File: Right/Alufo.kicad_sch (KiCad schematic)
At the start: 22 parts, among them J2 USB_C_Receptacle_USB2.0_16P_2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, J4 USB_C_Receptacle_USB2.0_16P_2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, SW10 BOOT, U2 CH552T, U4 USBLC6-2P6, U6 USBLC6-2P6

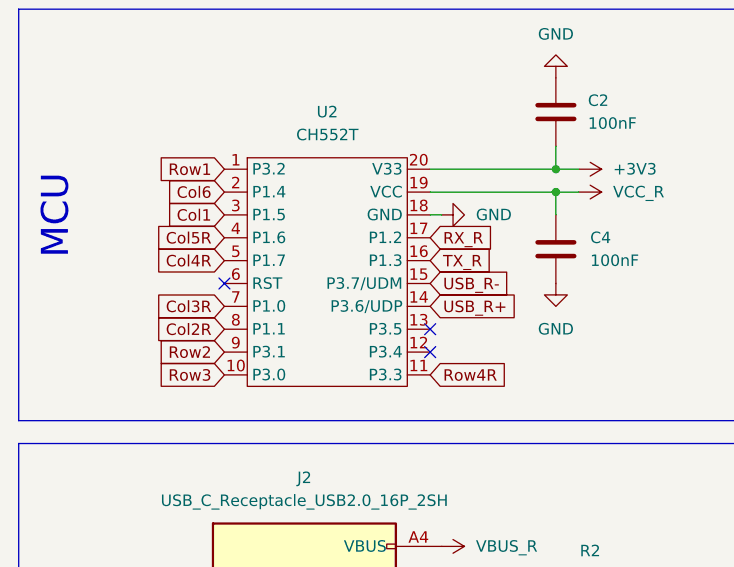
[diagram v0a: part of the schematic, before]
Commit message: Route Row 2 under upper 0Ω resistors
TODO: Reconnect Column 6 to thumb row
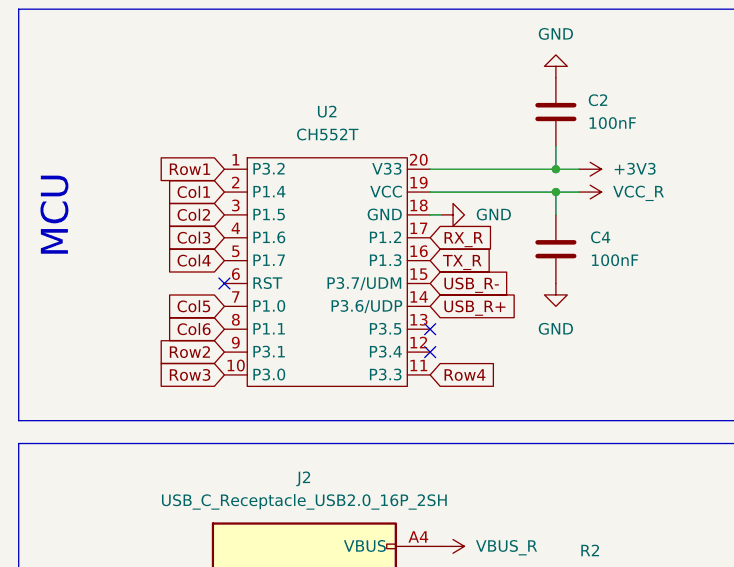
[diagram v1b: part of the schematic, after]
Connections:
- net Col2R is gone; now on net Col6: U2.8 (P1.1)
- net Col1: now also U2.2 (P1.4); no longer U2.3 (P1.5)
- net Col6: no longer U2.2 (P1.4)
- net Col3R renamed Col5
- net Col4R renamed Col4
- net Col5R renamed Col3
- net Row4R renamed Row4
- new net Col2: U2.3 (P1.5)
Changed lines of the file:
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@@
 		)
 	)
-	(global_label "Col5R"
+	(global_label "Col3"
 		(shape input)
 		(at 38.1 50.8 180)
@@
 		)
 		(property "Intersheetrefs" "${INTERSHEET_REFS}"
-			(at 29.5511 50.8 0)
+			(at 30.8211 50.8 0)
 			(effects
 				(font
@@
 		)
 	)
-	(global_label "Col4R"
+	(global_label "Col4"
 		(shape input)
 		(at 38.1 53.34 180)
@@
 		)
 		(property "Intersheetrefs" "${INTERSHEET_REFS}"
-			(at 29.5511 53.34 0)
-			(effects
-				(font
-					(size 1.27 1.27)
-				)
-				(justify right)
-				(hide yes)
-			)
-		)
-	)
-	(global_label "Row4R"
+			(at 30.8211 53.34 0)
+			(effects
+				(font
+					(size 1.27 1.27)
+				)
+				(justify right)
+				(hide yes)
+			)
+		)
+	)
+	(global_label "Row4"
 		(shape input)
 		(at 60.96 66.04 0)
@@
 		)
 		(property "Intersheetrefs" "${INTERSHEET_REFS}"
-			(at 70.1742 66.04 0)
-			(effects
-				(font
-					(size 1.27 1.27)
-				)
-				(justify left)
-				(hide yes)
-			)
-		)
-	)
-	(global_label "Col2R"
+			(at 68.9042 66.04 0)
+			(effects
+				(font
+					(size 1.27 1.27)
+				)
+				(justify left)
+				(hide yes)
+			)
+		)
+	)
+	(global_label "Col6"
 		(shape input)
 		(at 38.1 60.96 180)
@@
 		)
 		(property "Intersheetrefs" "${INTERSHEET_REFS}"
-			(at 29.5511 60.96 0)
+			(at 30.8211 60.96 0)
 			(effects
 				(font
@@
 		)
 	)
+	(global_label "Col2"
+		(shape input)
+		(at 38.1 48.26 180)
+		(fields_autoplaced yes)
+		(effects
+			(font
+				(size 1.27 1.27)
+			)
+			(justify right)
+		)
+		(property "Intersheetrefs" "${INTERSHEET_REFS}"
+			(at 30.8211 48.26 0)
+			(effects
+				(font
+					(size 1.27 1.27)
+				)
+				(justify right)
+				(hide yes)
+			)
+		)
+	)
+	(global_label "RX_PR"
+		(shape input)
+		(at 64.77 170.18 0)
+		(fields_autoplaced yes)
+		(effects
+			(font
+				(size 1.27 1.27)
+			)
+			(justify left)
+		)
+		(property "Intersheetrefs" "${INTERSHEET_REFS}"
+			(at 73.7423 170.18 0)
+			(effects
+				(font
+					(size 1.27 1.27)
+				)
+				(justify left)
+				(hide yes)
+			)
+		)
+	)
+	(global_label "USB_R-"
+		(shape input)
+		(at 115.57 115.57 180)
+		(fields_autoplaced yes)
+		(effects
+			(font
+				(size 1.27 1.27)
+			)
+			(justify right)
+		)
+		(property "Intersheetrefs" "${INTERSHEET_REFS}"
+			(at 104.9648 115.57 0)
+			(effects
+				(font
+					(size 1.27 1.27)
+				)
+				(justify right)
+				(hide yes)
+			)
+		)
+	)
+	(global_label "TX_PR"
+		(shape input)
+		(at 64.77 165.1 0)
+		(fields_autoplaced yes)
+		(effects
+			(font
+				(size 1.27 1.27)
+			)
+			(justify left)
+		)
+		(property "Intersheetrefs" "${INTERSHEET_REFS}"
+			(at 73.4399 165.1 0)
+			(effects
+				(font
+					(size 1.27 1.27)
+				)
+				(justify left)
+				(hide yes)
+			)
+		)
+	)
+	(global_label "BOOT"
+		(shape input)
+		(at 167.64 109.22 180)
+		(fields_autoplaced yes)
+		(effects
+			(font
+				(size 1.27 1.27)
+			)
+			(justify right)
+		)
+		(property "Intersheetrefs" "${INTERSHEET_REFS}"
+			(at 159.7562 109.22 0)
+			(effects
+				(font
+					(size 1.27 1.27)
+				)
+				(justify right)
+				(hide yes)
+			)
+		)
+	)
+	(global_label "Row1"
+		(shape input)
+		(at 38.1 43.18 180)
+		(fields_autoplaced yes)
+		(effects
+			(font
+				(size 1.27 1.27)
+			)
+			(justify right)
+		)
+		(property "Intersheetrefs" "${INTERSHEET_REFS}"
+			(at 30.1558 43.18 0)
+			(effects
+				(font
+					(size 1.27 1.27)
+				)
+				(justify right)
+				(hide yes)
+			)
+		)
+	)
 	(global_label "Col1"
 		(shape input)
-		(at 38.1 48.26 180)
-		(fields_autoplaced yes)
-		(effects
-			(font
-				(size 1.27 1.27)
-			)
-			(justify right)
-		)
-		(property "Intersheetrefs" "${INTERSHEET_REFS}"
-			(at 30.8211 48.26 0)
-			(effects
-				(font
-					(size 1.27 1.27)
-				)
-				(justify right)
-				(hide yes)
-			)
-		)
-	)
-	(global_label "RX_PR"
-		(shape input)
-		(at 64.77 170.18 0)
-		(fields_autoplaced yes)
-		(effects
-			(font
-				(size 1.27 1.27)
-			)
-			(justify left)
-		)
-		(property "Intersheetrefs" "${INTERSHEET_REFS}"
-			(at 73.7423 170.18 0)
-			(effects
-				(font
-					(size 1.27 1.27)
-				)
-				(justify left)
-				(hide yes)
-			)
-		)
-	)
-	(global_label "USB_R-"
-		(shape input)
-		(at 115.57 115.57 180)
-		(fields_autoplaced yes)
-		(effects
-			(font
-				(size 1.27 1.27)
-			)
-			(justify right)
-		)
-		(property "Intersheetrefs" "${INTERSHEET_REFS}"
-			(at 104.9648 115.57 0)
-			(effects
-				(font
-					(size 1.27 1.27)
-				)
-				(justify right)
-				(hide yes)
-			)
-		)
-	)
-	(global_label "TX_PR"
-		(shape input)
-		(at 64.77 165.1 0)
-		(fields_autoplaced yes)
-		(effects
-			(font
-				(size 1.27 1.27)
-			)
-			(justify left)
-		)
-		(property "Intersheetrefs" "${INTERSHEET_REFS}"
-			(at 73.4399 165.1 0)
-			(effects
-				(font
-					(size 1.27 1.27)
-				)
-				(justify left)
-				(hide yes)
-			)
-		)
-	)
-	(global_label "BOOT"
-		(shape input)
-		(at 167.64 109.22 180)
-		(fields_autoplaced yes)
-		(effects
-			(font
-				(size 1.27 1.27)
-			)
-			(justify right)
-		)
-		(property "Intersheetrefs" "${INTERSHEET_REFS}"
-			(at 159.7562 109.22 0)
-			(effects
-				(font
-					(size 1.27 1.27)
-				)
-				(justify right)
-				(hide yes)
-			)
-		)
-	)
-	(global_label "Row1"
-		(shape input)
-		(at 38.1 43.18 180)
-		(fields_autoplaced yes)
-		(effects
-			(font
-				(size 1.27 1.27)
-			)
-			(justify right)
-		)
-		(property "Intersheetrefs" "${INTERSHEET_REFS}"
-			(at 30.1558 43.18 0)
-			(effects
-				(font
-					(size 1.27 1.27)
-				)
-				(justify right)
-				(hide yes)
-			)
-		)
-	)
-	(global_label "Col6"
-		(shape input)
 		(at 38.1 45.72 180)
 		(fields_autoplaced yes)
@@
 		)
 	)
-	(global_label "Col3R"
+	(global_label "Col5"
 		(shape input)
 		(at 38.1 58.42 180)
@@
 		)
 		(property "Intersheetrefs" "${INTERSHEET_REFS}"
-			(at 29.5511 58.42 0)
-			(effects
-				(font
+			(at 30.8211 58.42 0)
+			(effects
+				(font

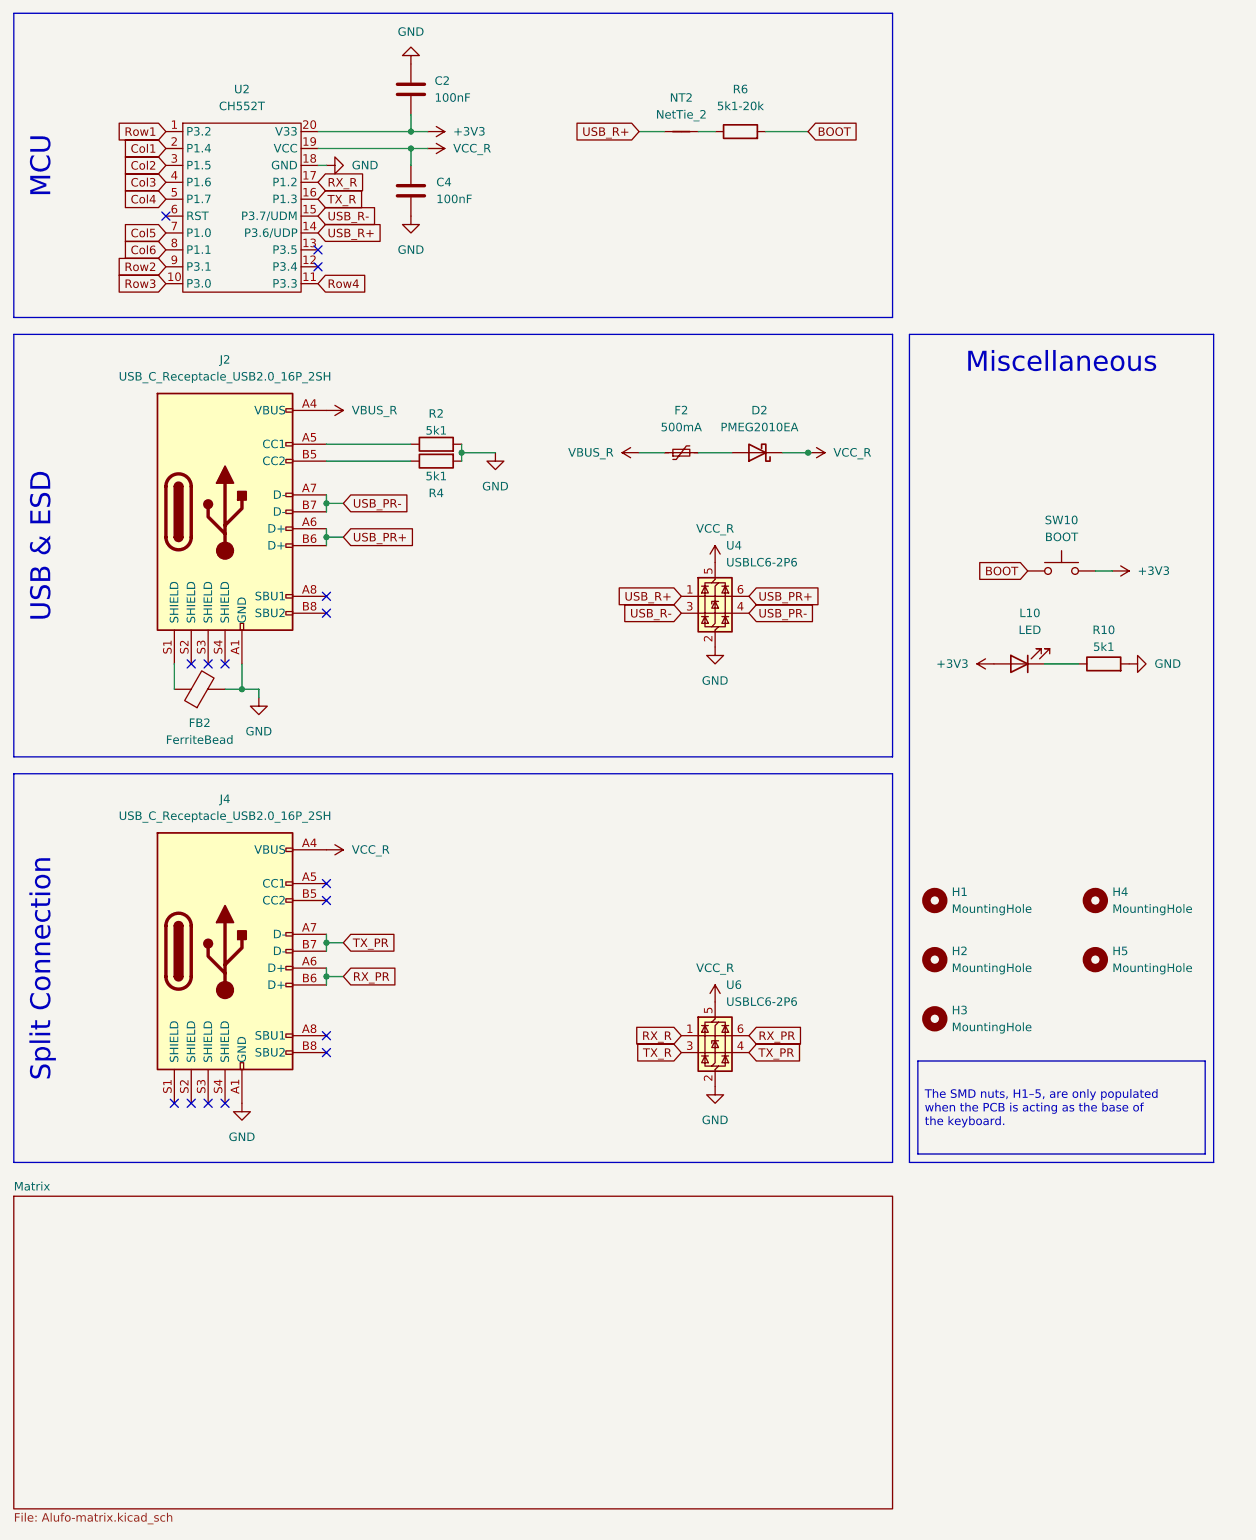
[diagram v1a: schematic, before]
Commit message: Remove “L” and “R” from all labels
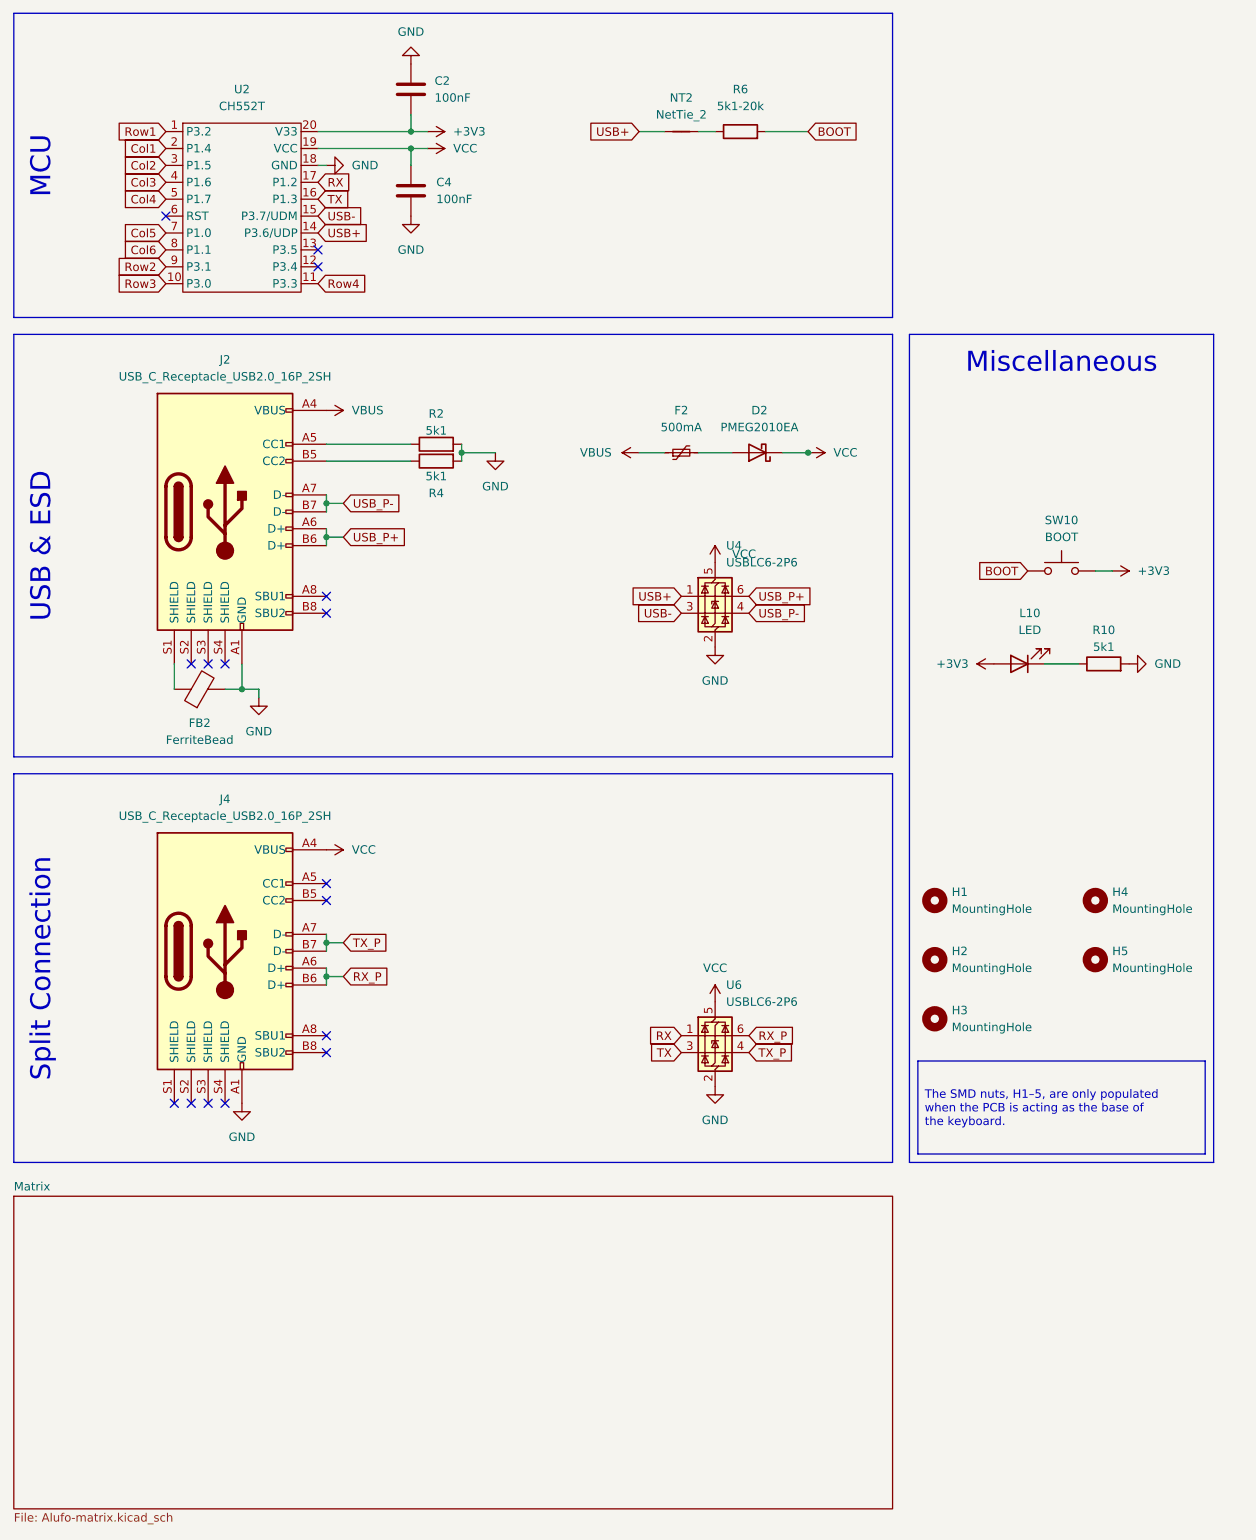
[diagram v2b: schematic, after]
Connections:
- net RX_PR renamed RX_P
- net RX_R renamed RX
- net TX_PR renamed TX_P
- net TX_R renamed TX
- net USB_PR+ renamed USB_P+
- net USB_PR- renamed USB_P-
- net USB_R+ renamed USB+
- net USB_R- renamed USB-
- net VBUS_R renamed VBUS
- net VCC_R renamed VCC
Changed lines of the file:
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@@
 		)
 	)
-	(global_label "USB_R-"
+	(global_label "USB-"
 		(shape input)
 		(at 60.96 55.88 0)
@@
 		)
 		(property "Intersheetrefs" "${INTERSHEET_REFS}"
-			(at 71.5652 55.88 0)
-			(effects
-				(font
-					(size 1.27 1.27)
-				)
-				(justify left)
-				(hide yes)
-			)
-		)
-	)
-	(global_label "RX_PR"
+			(at 69.3276 55.88 0)
+			(effects
+				(font
+					(size 1.27 1.27)
+				)
+				(justify left)
+				(hide yes)
+			)
+		)
+	)
+	(global_label "RX_P"
 		(shape input)
 		(at 125.73 179.07 0)
@@
 		)
 		(property "Intersheetrefs" "${INTERSHEET_REFS}"
-			(at 134.7023 179.07 0)
+			(at 133.4323 179.07 0)
 			(effects
 				(font
@@
 		)
 	)
-	(global_label "TX_R"
+	(global_label "TX"
 		(shape input)
 		(at 60.96 53.34 0)
@@
 		)
 		(property "Intersheetrefs" "${INTERSHEET_REFS}"
-			(at 68.3599 53.34 0)
-			(effects
-				(font
-					(size 1.27 1.27)
-				)
-				(justify left)
-				(hide yes)
-			)
-		)
-	)
-	(global_label "RX_R"
+			(at 66.1223 53.34 0)
+			(effects
+				(font
+					(size 1.27 1.27)
+				)
+				(justify left)
+				(hide yes)
+			)
+		)
+	)
+	(global_label "RX"
 		(shape input)
 		(at 115.57 179.07 180)
@@
 		)
 		(property "Intersheetrefs" "${INTERSHEET_REFS}"
-			(at 107.8677 179.07 0)
+			(at 110.1053 179.07 0)
 			(effects
 				(font
@@
 		)
 	)
-	(global_label "TX_PR"
+	(global_label "TX_P"
 		(shape input)
 		(at 125.73 181.61 0)
@@
 		)
 		(property "Intersheetrefs" "${INTERSHEET_REFS}"
-			(at 134.3999 181.61 0)
-			(effects
-				(font
-					(size 1.27 1.27)
-				)
-				(justify left)
-				(hide yes)
-			)
-		)
-	)
-	(global_label "USB_PR-"
+			(at 133.1299 181.61 0)
+			(effects
+				(font
+					(size 1.27 1.27)
+				)
+				(justify left)
+				(hide yes)
+			)
+		)
+	)
+	(global_label "USB_P-"
 		(shape input)
 		(at 64.77 99.06 0)
@@
 		)
 		(property "Intersheetrefs" "${INTERSHEET_REFS}"
-			(at 76.6452 99.06 0)
+			(at 75.3752 99.06 0)
 			(effects
 				(font
@@
 		)
 	)
-	(global_label "USB_PR-"
+	(global_label "USB_P-"
 		(shape input)
 		(at 125.73 115.57 0)
@@
 		)
 		(property "Intersheetrefs" "${INTERSHEET_REFS}"
-			(at 137.6052 115.57 0)
-			(effects
-				(font
-					(size 1.27 1.27)
-				)
-				(justify left)
-				(hide yes)
-			)
-		)
-	)
-	(global_label "USB_PR+"
+			(at 136.3352 115.57 0)
+			(effects
+				(font
+					(size 1.27 1.27)
+				)
+				(justify left)
+				(hide yes)
+			)
+		)
+	)
+	(global_label "USB_P+"
 		(shape input)
 		(at 125.73 113.03 0)
@@
 		)
 		(property "Intersheetrefs" "${INTERSHEET_REFS}"
-			(at 137.6052 113.03 0)
-			(effects
-				(font
-					(size 1.27 1.27)
-				)
-				(justify left)
-				(hide yes)
-			)
-		)
-	)
-	(global_label "USB_R+"
+			(at 136.3352 113.03 0)
+			(effects
+				(font
+					(size 1.27 1.27)
+				)
+				(justify left)
+				(hide yes)
+			)
+		)
+	)
+	(global_label "USB+"
 		(shape input)
 		(at 60.96 58.42 0)
@@
 		)
 		(property "Intersheetrefs" "${INTERSHEET_REFS}"
-			(at 71.5652 58.42 0)
+			(at 69.3276 58.42 0)
 			(effects
 				(font
@@
 		)
 	)
-	(global_label "USB_R+"
+	(global_label "USB+"
 		(shape input)
 		(at 109.22 43.18 180)
@@
 		)
 		(property "Intersheetrefs" "${INTERSHEET_REFS}"
-			(at 98.6148 43.18 0)
+			(at 100.8524 43.18 0)
 			(effects
 				(font
@@
 		)
 	)
-	(global_label "USB_PR+"
+	(global_label "USB_P+"
 		(shape input)
 		(at 64.77 104.14 0)
@@
 		)
 		(property "Intersheetrefs" "${INTERSHEET_REFS}"
-			(at 76.6452 104.14 0)
+			(at 75.3752 104.14 0)
 			(effects
 				(font
@@
 		)
 	)
-	(global_label "USB_R+"
+	(global_label "USB+"
 		(shape input)
 		(at 115.57 113.03 180)
@@
 		)
 		(property "Intersheetrefs" "${INTERSHEET_REFS}"
-			(at 104.9648 113.03 0)
+			(at 107.2024 113.03 0)
 			(effects
 				(font
@@
 		)
 	)
-	(global_label "RX_PR"
+	(global_label "RX_P"
 		(shape input)
 		(at 64.77 170.18 0)
@@
 		)
 		(property "Intersheetrefs" "${INTERSHEET_REFS}"
-			(at 73.7423 170.18 0)
-			(effects
-				(font
-					(size 1.27 1.27)
-				)
-				(justify left)
-				(hide yes)
-			)
-		)
-	)
-	(global_label "USB_R-"
+			(at 72.4723 170.18 0)
+			(effects
+				(font
+					(size 1.27 1.27)
+				)
+				(justify left)
+				(hide yes)
+			)
+		)
+	)
+	(global_label "USB-"
 		(shape input)
 		(at 115.57 115.57 180)
@@
 		)
 		(property "Intersheetrefs" "${INTERSHEET_REFS}"
-			(at 104.9648 115.57 0)
+			(at 107.2024 115.57 0)
 			(effects
 				(font
@@
 		)
 	)
-	(global_label "TX_PR"
+	(global_label "TX_P"
 		(shape input)
 		(at 64.77 165.1 0)
@@
 		)
 		(property "Intersheetrefs" "${INTERSHEET_REFS}"
-			(at 73.4399 165.1 0)
+			(at 72.1699 165.1 0)
 			(effects
 				(font
@@
 		)
 	)
-	(global_label "RX_R"
+	(global_label "RX"
 		(shape input)
 		(at 60.96 50.8 0)
@@
 		)
 		(property "Intersheetrefs" "${INTERSHEET_REFS}"
-			(at 68.6623 50.8 0)
-			(effects
-				(font
-					(size 1.27 1.27)
-				)
-				(justify left)
-				(hide yes)
-			)
-		)
-	)
-	(global_label "TX_R"
+			(at 66.4247 50.8 0)
+			(effects
+				(font
+					(size 1.27 1.27)
+				)
+				(justify left)
+				(hide yes)
+			)
+		)
+	)
+	(global_label "TX"
 		(shape input)
 		(at 115.57 181.61 180)
@@
 		)
 		(property "Intersheetrefs" "${INTERSHEET_REFS}"
-			(at 108.1701 181.61 0)
+			(at 110.4077 181.61 0)
 			(effects
 				(font
@@
 			)
 		)
-		(property "Value" "VCC_R"
+		(property "Value" "VCC"
 			(at 138.43 91.4399 90)
 			(effects
@@
 			)
 		)
-		(property "Value" "VCC_R"
+		(property "Value" "VCC"
 			(at 120.65 168.91 0)
 			(effects
@@
 			)
 		)
-		(property "Value" "VBUS_R"
+		(property "Value" "VBUS"
 			(at 66.04 85.0899 90)
 			(effects
@@
 			)
 		)
-		(property "Value" "VCC_R"
-			(at 120.65 102.87 0)
-			(effects
-				(font
-					(size 1.27 1.27)
-				)
+		(property "Value" "VCC"
+			(at 123.19 106.6799 0)
+			(effects
+				(font
+					(size 1.27 1.27)
+				)
+				(justify left)
 			)
 		)
@@
 		(on_board yes)
 		(dnp no)
-		(fields_autoplaced yes)
 		(property "Reference" "#PWR034"
 			(at 113.03 91.44 0)
@@
 			)
 		)
-		(property "Value" "VBUS_R"
-			(at 105.41 91.4399 90)
-			(effects
-				(font
-					(size 1.27 1.27)
-				)
-				(justify left)
+		(property "Value" "VBUS"
+			(at 100.33 91.44 90)
+			(effects
+				(font
+					(size 1.27 1.27)
+				)
+				(justify right)
 			)
 		)
@@
 			)
 		)
-		(property "Value" "VCC_R"
+		(property "Value" "VCC"
 			(at 81.28 45.7199 90)
 			(effects
@@
 			)
 		)
-		(property "Value" "VCC_R"
+		(property "Value" "VCC"
 			(at 66.04 151.1299 90)
 			(effects
